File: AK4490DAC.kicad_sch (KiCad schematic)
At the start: 78 parts, among them IC1 LP5907MFX-3.3/NOPB, IC2 LP5907MFX-3.3/NOPB, IC3 LP5907MFX-3.3/NOPB, IC4 TPS7A2050PDBVR, IC5 MUSES8920, IC6 MUSES8920, IC7 MUSES8920, IC8 TPS7A2050PDBVR, IC9 AMS1117, J1 JST_XA_B02B-XASK-1, J2 USB_B_Micro, J3 SPDIF_IN, J4 LINE_OUT_L, J5 LINE_OUT_R, Q1 BSS138, T1 DA103C, U1 SN74LS06NSR, U2 PCM2704CDBR, U3 TCM809TENB713, U4 TCM809TENB713, U5 AK4118, U6 AK4490, Y1 11.2896MHz, Y2 12MHz

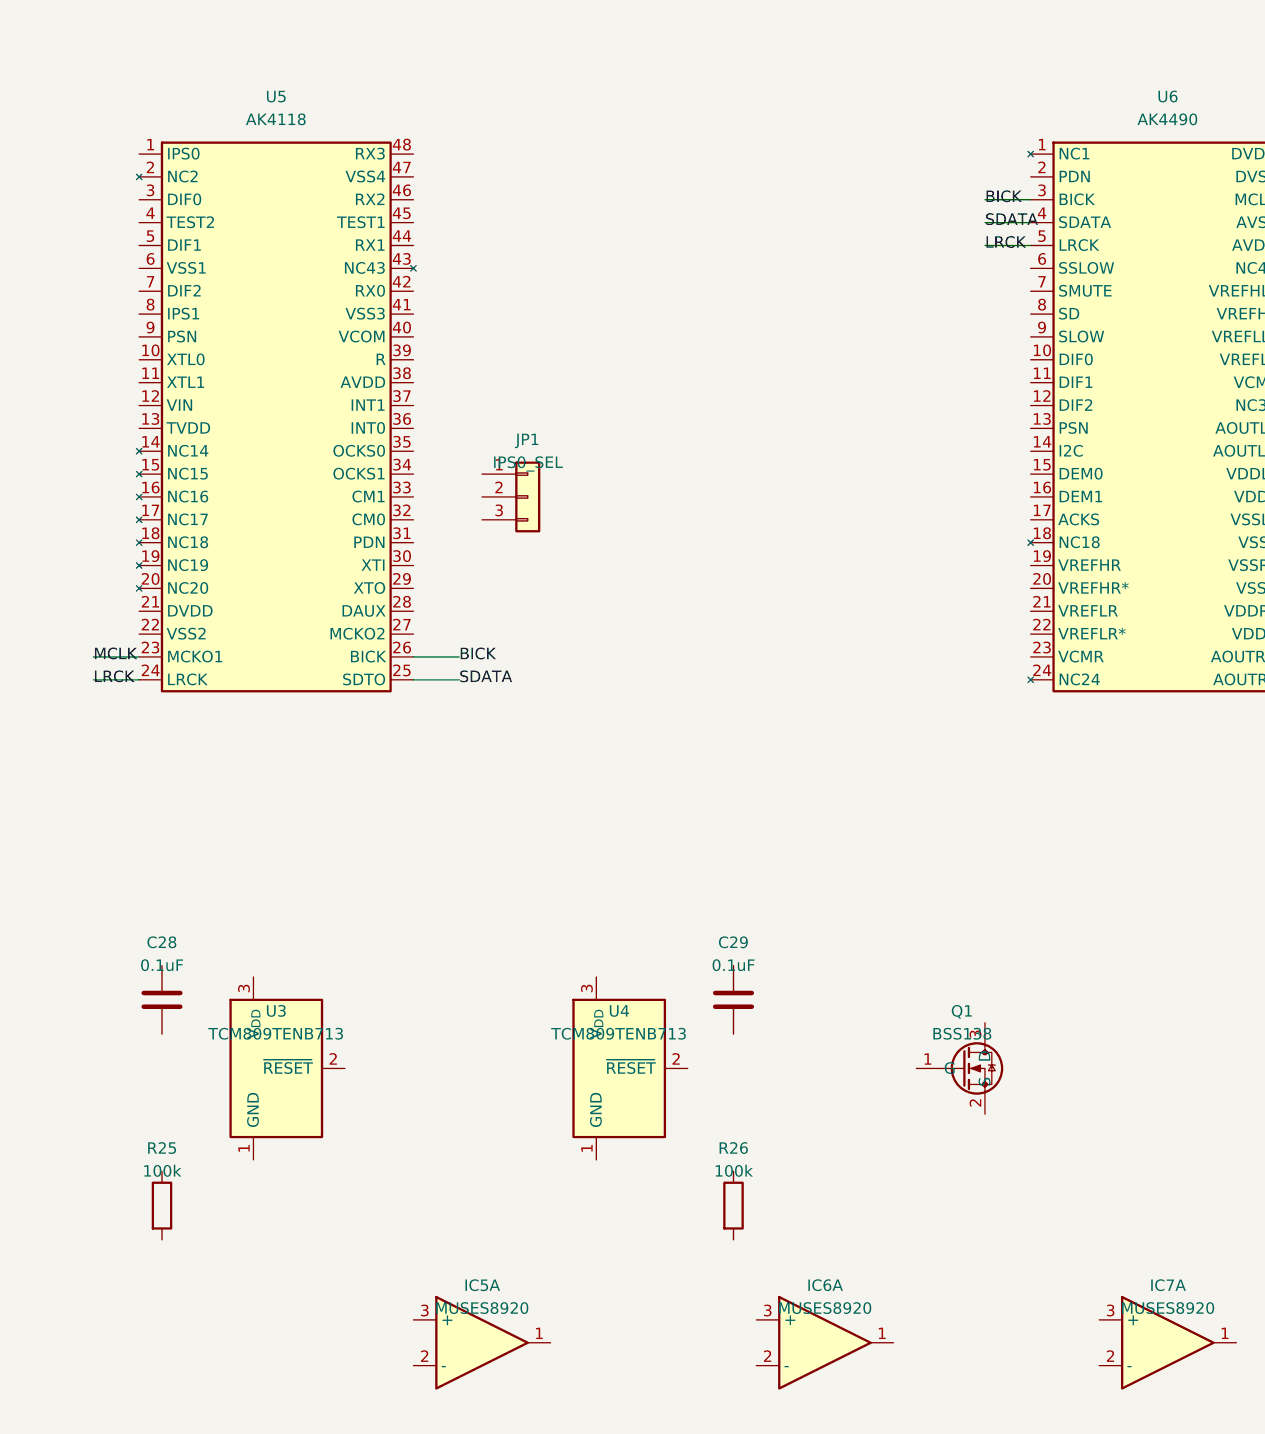
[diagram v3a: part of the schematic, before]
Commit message: Verify TCM809T reset supervisor selection and wire it into the circuit
Verification against Microchip datasheet DS21661E and the AK4118/
AK4490 datasheets (both require PDN = "L" held during power-up, then
released to "H" once supply is stable -- Mouser AK4118A datasheet;
AKM AK4490 datasheet MS1648-E-03):

- Necessity: confirmed genuinely required, not just convention -- both
  DACs need an active power-on reset pulse on PDN, not a static tie.
- Threshold: TCM809T (3.00-3.15V) matches the monitored 3.3V DVDD
  rails per Microchip's own "VDD=3.3V for T/S" pairing (fixed last
  commit).
- Timing margin: TCM809's 140ms minimum RESET-active period vastly
  exceeds AK4490's 150ns minimum PDN pulse width (tPD) -- no conflict.
- Output type: push-pull active-low RESET drives PDN directly with no
  extra components needed beyond the datasheet-recommended pull-down/
  decoupling already added.
- Package/cost: SOT-23-3, hand-solderable, consistent with the rest of
  this design's cost-conscious part selection.

No issues found, so wired it into the schematic (previously placed but
fully unconnected):
  U3 (AK4118 reset):  VDD->+3V3_118, GND->GND, RESET->RST_118
  R25 (100k pulldown): RST_118 <-> GND
  C28 (0.1uF decouple): +3V3_118 <-> GND
  AK4118 PDN (pin 31) -> RST_118

  U4 (AK4490 reset):  VDD->+3V3_4490, GND->GND, RESET->RST_4490
  R26 (100k pulldown): RST_4490 <-> GND
  C29 (0.1uF decouple): +3V3_4490 <-> GND
  AK4490 PDN (pin 2) -> RST_4490

Net names +3V3_118/+3V3_4490 are the connection points the user should
also use when wiring the LP5907 regulator outputs to each DAC's DVDD.

All 16 new connections use the project's existing local-label wiring
style (short stub wire + label at the pin), the same pattern already
used for the BICK/LRCK/SDATA/MCLK links -- pin absolute coordinates
derived from each symbol's placement + its pin's relative offset
(schematic Y is flipped vs. symbol-space Y: y_abs = symbol_y - pin_y).

Verified via kicad-cli sch erc: 365 violations (do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
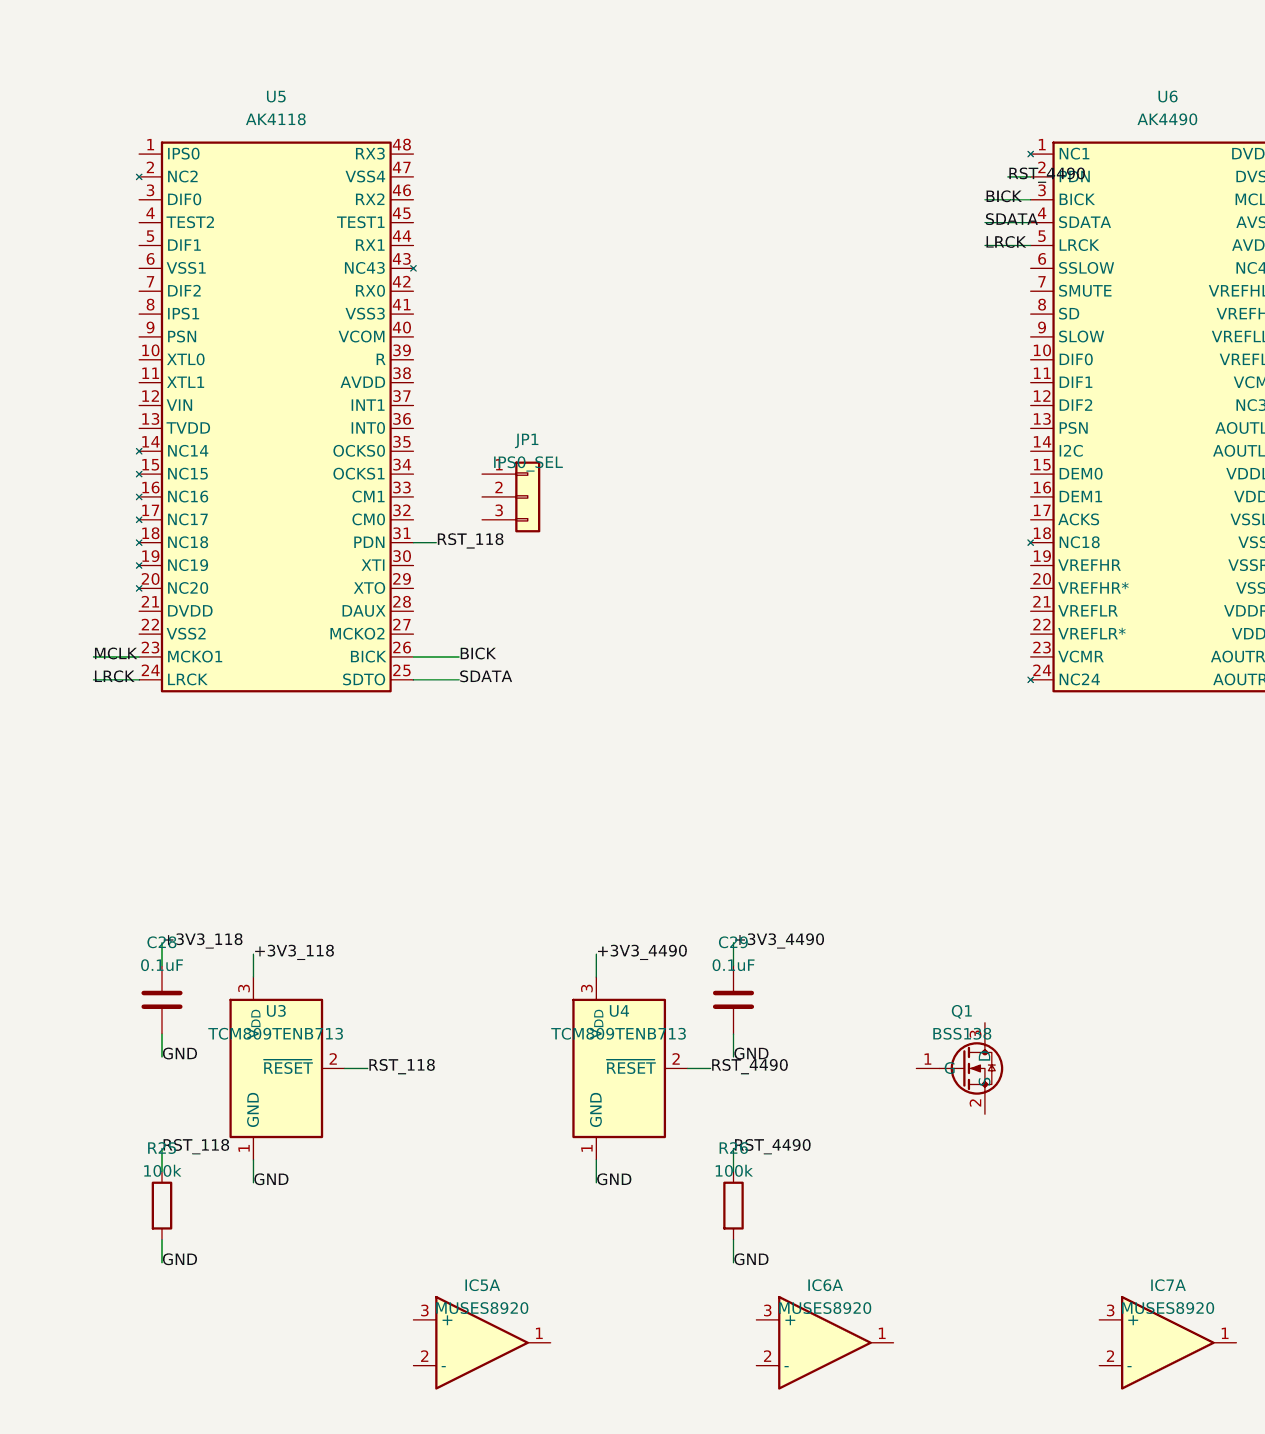
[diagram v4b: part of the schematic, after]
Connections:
- net RST_118: now reaches U5.31 (PDN)
- net RST_118: now also R25.1, U3.2 (~{RESET})
- net GND: now reaches U3.1 (GND)
- net GND: now also C28.2, C29.2, R25.2, R26.2, U4.1 (GND)
- net +3V3_118: now reaches U3.3 (V_{DD})
- net +3V3_118: now also C28.1
- net RST_4490: now reaches R26.1
- net RST_4490: now also U4.2 (~{RESET}), U6.2 (PDN)
- net +3V3_4490: now reaches U4.3 (V_{DD})
- net +3V3_4490: now also C29.1

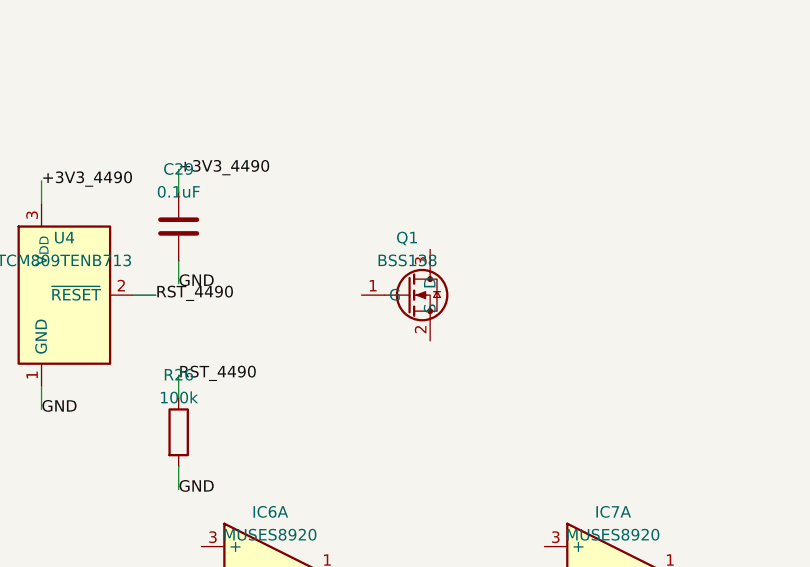
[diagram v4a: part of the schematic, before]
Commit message: Remove Q1 (BSS138): orphaned leftover from the abandoned SA9227 design
Audited Q1 the same way as the TCM809 reset ICs. Findings:
- Added in ed632a9 ("Upgrade design: SA9227 USB async audio, ADP7142
  LDOs, MUSES8920 op-amps") alongside SA9227/24LC02/74LS157, but never
  mentioned in that commit's message, and its Description property was
  left blank.
- Never wired to anything at any point in this repo's history (checked
  every commit touching AK4490DAC.kicad_sch) -- zero net connections,
  ever.
- SA9227/24LC02/74LS157 were explicitly removed together in 4d609bf
  once the direction changed to external USB-SPDIF, but Q1 was missed
  from that removal list.

BSS138 is a classic bidirectional I2C level-shifter FET (e.g. NXP
AN97055), which fits a system built around SA9227 + a 24LC02 EEPROM on
a different voltage domain -- but with both of those already gone,
Q1 has no remaining role in the current design. Removing it (component
instance + its lib_symbols cache entry; nothing else referenced it).

Note: this also happens to drop lib_symbol_mismatch from 5 to 4, i.e.
BSS138's hand-typed cache entry was itself one of the pre-existing
baseline mismatches.

(First attempt at this removal had an off-by-one in the block-boundary
search -- `rfind('(symbol', 0, idx)` treated the match position as
excluded, so it walked back to an unrelated symbol (Transformer:
TRANSF1's inner unit) instead. Caught it via git diff before verifying
ERC, reverted, and fixed the boundary logic before redoing it.)

Verified via kicad-cli sch erc: 361 violations, lib_symbol_mismatch=4,
no crash. Diff confirmed to touch only the BSS138 cache block and the
Q1 instance.

Co-Authored-By: Claude Sonnet 5 <noreply@anthropic.com>
Claude-Session: https://claude.ai/code/session_01UHxU1bYnUhoAmCyc4Koj96
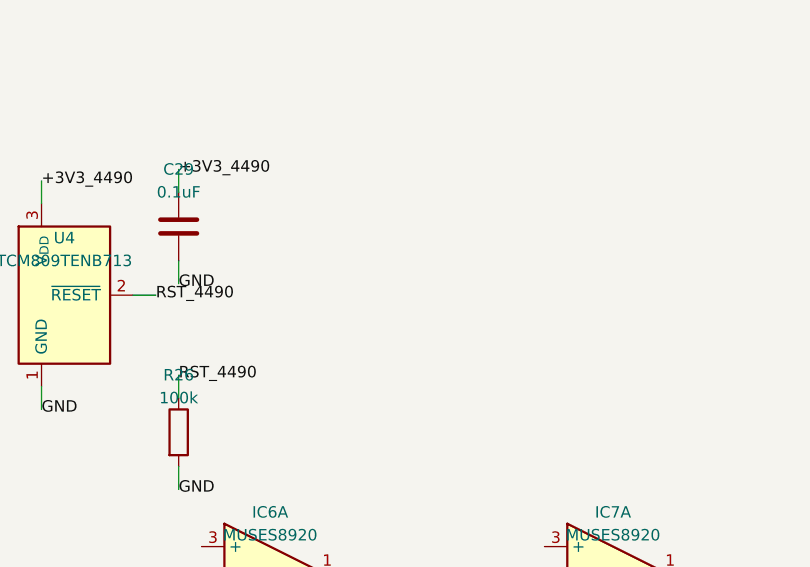
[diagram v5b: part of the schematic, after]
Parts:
- removed Q1: BSS138, Package_TO_SOT_SMD:SOT-23, symbol Transistor_FET:BSS138
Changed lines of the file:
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@@
-	)
-	(symbol
-		(lib_id "Transistor_FET:BSS138")
-		(at 307.34 203.2 0)
-		(unit 1)
-		(exclude_from_sim no)
-		(in_bom yes)
-		(on_board yes)
-		(dnp no)
-		(property "Reference" "Q1"
-			(at 307.34 196.85 0)
-			(effects
-				(font
-					(size 1.27 1.27)
-				)
-			)
-		)
-		(property "Value" "BSS138"
-			(at 307.34 199.39 0)
-			(effects
-				(font
-					(size 1.27 1.27)
-				)
-			)
-		)
-		(property "Footprint" "Package_TO_SOT_SMD:SOT-23"
-			(at 307.34 203.2 0)
-			(effects
-				(font
-					(size 1.27 1.27)
-				)
-				(hide yes)
-			)
-		)
-		(property "Datasheet" ""
-			(at 307.34 203.2 0)
-			(effects
-				(font
-					(size 1.27 1.27)
-				)
-				(hide yes)
-			)
-		)
-		(property "Description" ""
-			(at 307.34 203.2 0)
-			(effects
-				(font
-					(size 1.27 1.27)
-				)
-			)
-		)
-		(pin "1"
-		)
-		(pin "2"
-		)
-		(pin "3"
-		)
-		(instances
-			(project "AK4490DAC"
-				(path "/43171a2d-7dc9-4067-85e7-263b74d7a8f4"
-					(reference "Q1")
-					(unit 1)
-				)
-			)
-		)
 	)
 	(symbol
